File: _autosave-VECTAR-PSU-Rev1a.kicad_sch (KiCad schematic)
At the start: 63 parts, among them J1 XT60PW-M, J2 XT60PW-M, J3 Conn_01x02_Socket, J5 Conn_01x06_Socket, J6 XT90PW-M, Q1 2N7002, Q2 IRFB7437, Q3 IRFB7437, SW2 RA1113112R, U1 LM74502DDFR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

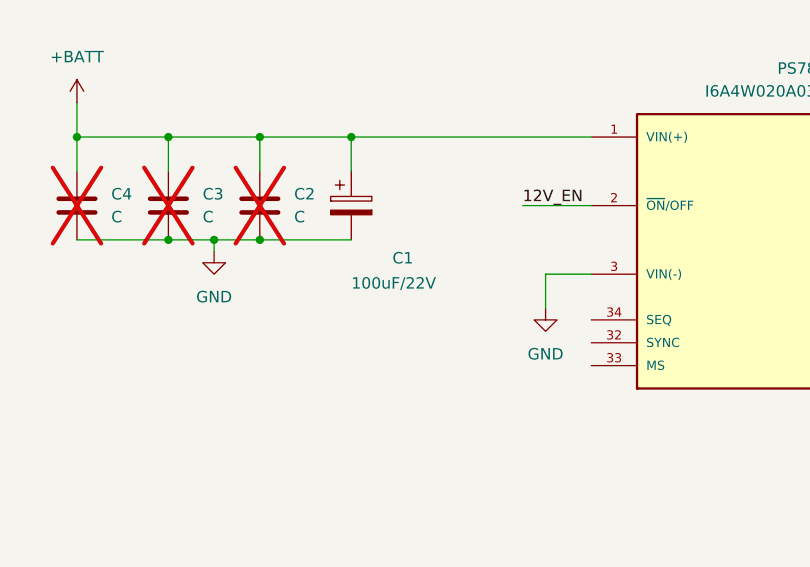
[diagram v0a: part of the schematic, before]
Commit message: Added ideal diode controller, still not done
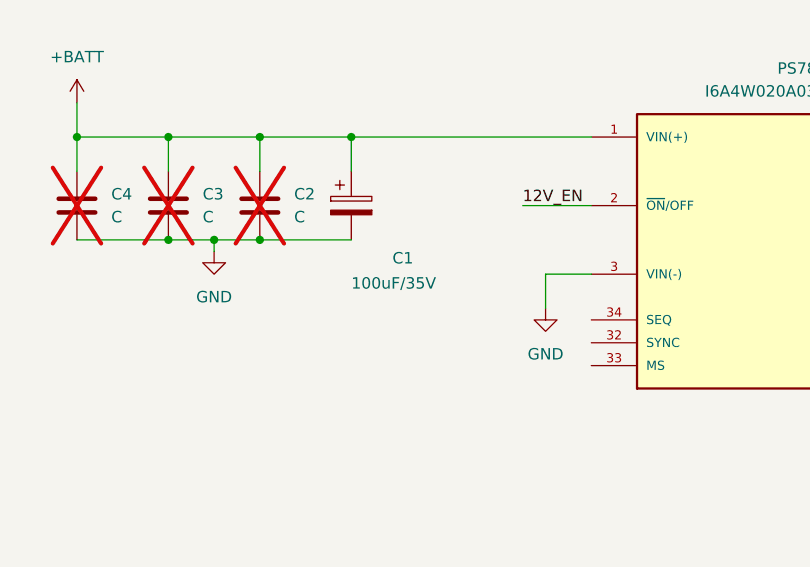
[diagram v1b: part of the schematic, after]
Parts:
- C1: value 100uF/22V -> 100uF/35V
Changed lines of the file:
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@@
 			)
 		)
-		(property "Value" "100uF/22V"
+		(property "Value" "100uF/35V"
 			(at 243.84 101.346 0)
 			(effects
@@
 			)
 		)
-		(property "Datasheet" "~"
+		(property "Datasheet" "https://www.eaton.com/content/dam/eaton/products/electronic-components/resources/data-sheet/eaton-ehbsa-hybrid-aluminum-electrolytic-capacitor-data-sheet-elx1481-en.pdf"
 			(at 243.84 92.71 0)
 			(effects
